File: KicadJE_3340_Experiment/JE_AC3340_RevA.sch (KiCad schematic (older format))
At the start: 99 parts

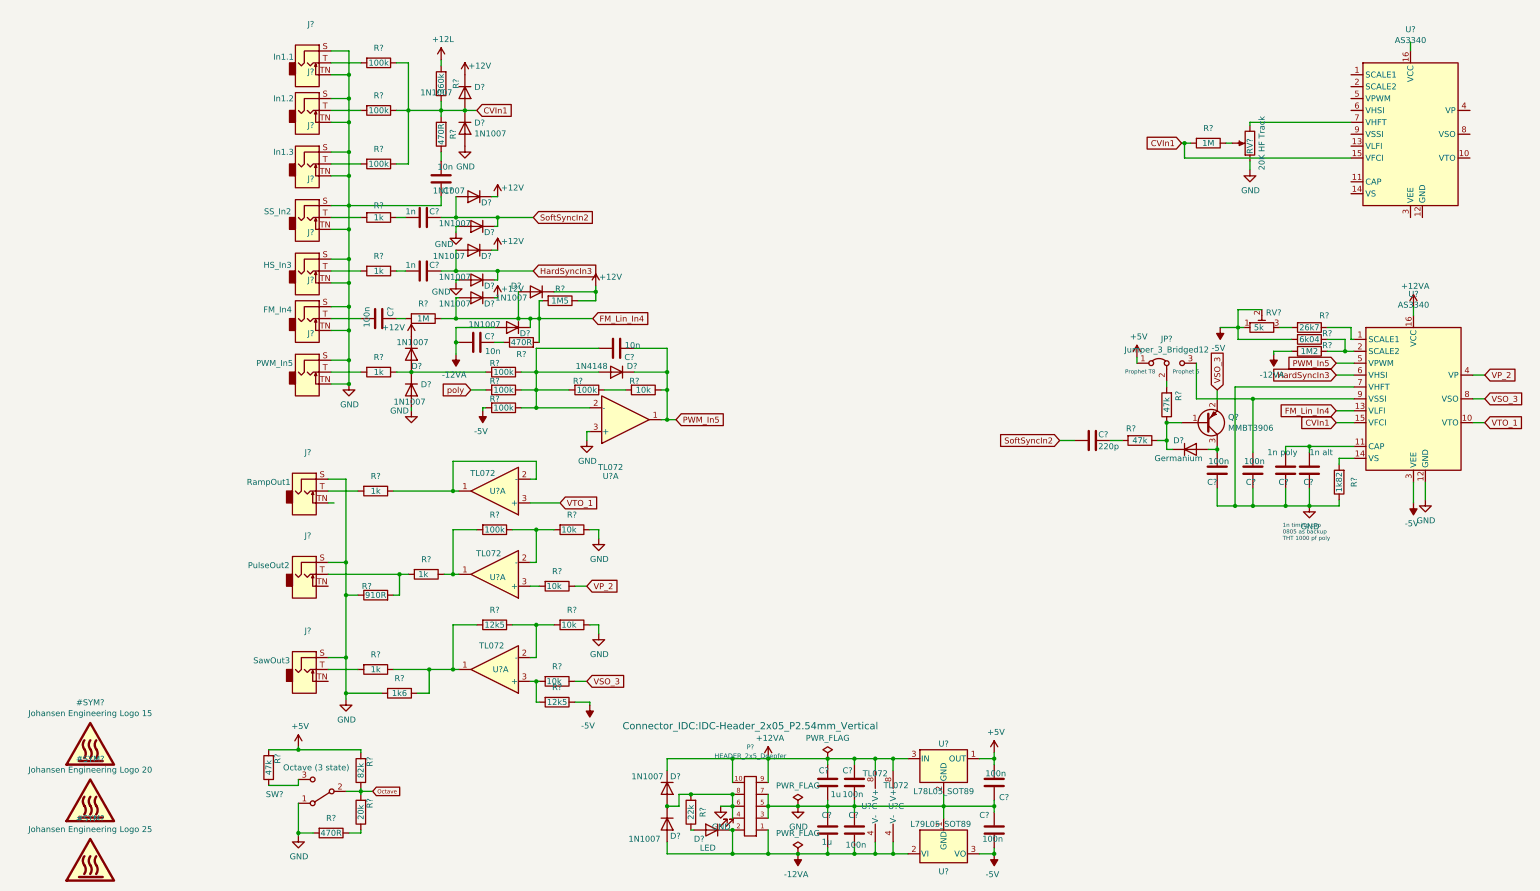
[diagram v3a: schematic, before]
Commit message: Label JE 3 + Pot's
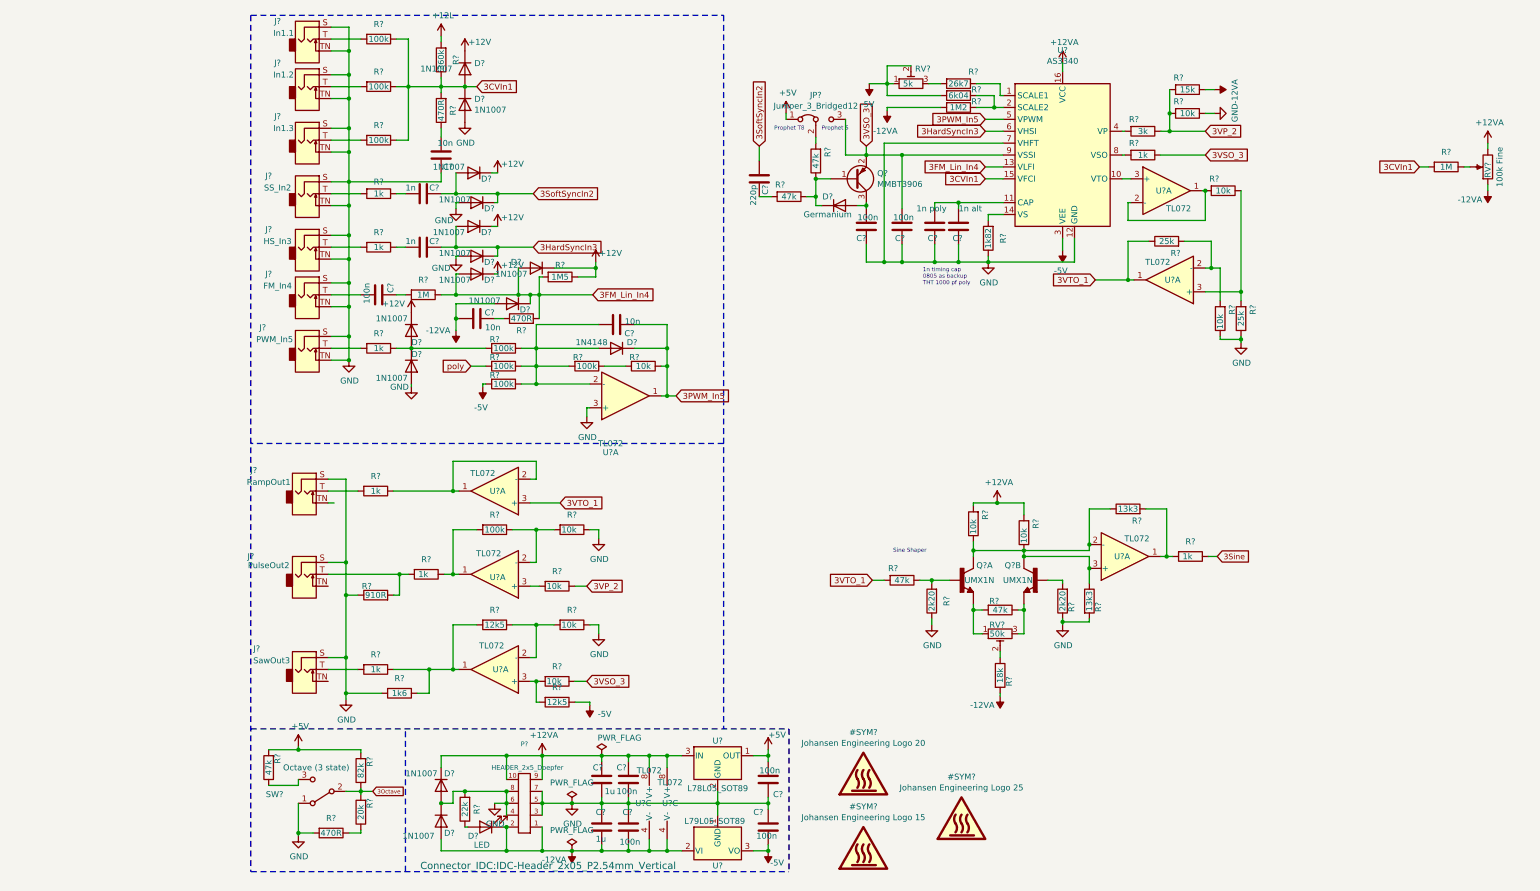
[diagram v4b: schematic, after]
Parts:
- removed U?: AS3340, symbol Audio:AS3340
- added Q? (x2): UMX1N, UMT6, symbol UMX1N:UMX1N
- added R?: 3k, Resistor_SMD:R_0805_2012Metric_Pad1.15x1.40mm_HandSolder, symbol Device:R
- added R? (x2): 1k, Resistor_SMD:R_0805_2012Metric_Pad1.15x1.40mm_HandSolder, symbol Device:R
- added R? (x5): 10k, Resistor_SMD:R_0805_2012Metric_Pad1.15x1.40mm_HandSolder, symbol Device:R
- added R?: 15k, Resistor_SMD:R_0805_2012Metric_Pad1.15x1.40mm_HandSolder, symbol Device:R
- added R? (x2): 25k, Resistor_SMD:R_0805_2012Metric_Pad1.15x1.40mm_HandSolder, symbol Device:R
- added R? (x2): 47k, Resistor_SMD:R_0805_2012Metric_Pad1.15x1.40mm_HandSolder, symbol Device:R
- added R? (x2): 2k20, Resistor_SMD:R_0805_2012Metric_Pad1.15x1.40mm_HandSolder, symbol Device:R
- added R? (x2): 13k3, Resistor_SMD:R_0805_2012Metric_Pad1.15x1.40mm_HandSolder, symbol Device:R
- added R?: 18k, Resistor_SMD:R_0805_2012Metric_Pad1.15x1.40mm_HandSolder, symbol Device:R
- added RV?: 50k, Potentiometer_THT:Potentiometer_Bourns_3296W_Vertical, symbol Device:R_POT_TRIM
- added U? (x3): TL072, AJ-Dropbox-Kicad:AJ_SO-8_5.3x6.2mm_P1.27mm, symbol Amplifier_Operational:TL072
- RV?: value 20K HF Track -> 100k Fine
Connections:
- net +12VA: now also RV?.3, R?.2, R?.2
- net -12VA: now also RV?.1, R?.1, R?.2
- net GND: now also R?.1, R?.1, R?.1, R?.1, R?.1, R?.2; no longer RV?.1
- net 3VSO_3: now reaches C?.2, JP?.3 (B), U?.9 (VSSI)
- net 3VSO_3: now also Q?.2 (E), R?.1, R?.1
- net CVIn1 renamed 3CVIn1
- net FM_Lin_In4 renamed 3FM_Lin_In4
- net HardSyncIn3 renamed 3HardSyncIn3
- net Octave renamed 3Octave
- net PWM_In5 renamed 3PWM_In5
- net SoftSyncIn2 renamed 3SoftSyncIn2
- net VP_2: no longer names the net of U?.4 (VP)
- net VP_2: now also R?.2; no longer R?.1
- removed net VSO_3: Q?.2 (E), R?.1, U?.8 (VSO)
- net VTO_1: no longer names the net of U?.10 (VTO)
- net VTO_1: now also U?.3 (+); no longer U?.3 (+)
- new net: R?.2, U?.8 (VSO)
- new net: R?.2, U?.1, U?.2 (-)
- new net: R?.2, R?.2, U?.2 (-)
- new net: R?.1, R?.2, U?.3 (+)
- new net: Q?.2 (B), R?.1, R?.2
- new net: Q?.1 (E), R?.2, RV?.1
- new net: Q?.3 (C), Q?.6 (C), R?.1, R?.1, R?.1, R?.1, U?.2 (-), U?.3 (+)
- new net: Q?.4 (E), R?.1, RV?.3
- new net: Q?.5 (B), R?.2
- new net: R?.2, R?.2, U?.1
- new net: R?.1, RV?.2
- new net 3Sine: R?.1
- new net 3VP_2: R?.1, R?.1, R?.2, R?.2
- new net 3VTO_1: R?.1, R?.2, U?.1, U?.3 (+)
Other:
- note added: "Sine Shaper"
- moved on the sheet: C?, D?, J?, JP?, P?, Q?, R?, RV?, U?, U?A, U?C

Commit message: Update JE_AC3340_RevA.sch
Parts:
- added D? (x2): 1N1007, Diode_SMD:D_SOD-123, symbol Device:D
- added R?: 100k, Resistor_SMD:R_0805_2012Metric_Pad1.15x1.40mm_HandSolder, symbol Device:R
- added RV?: 100k PWM, AJ-Dropbox-Kicad:Potentiometer_China_RK09_Single_Vertical_AJ, symbol Envelope-cache-2018-08-04-13-00-04:POT
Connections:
- net +12VA: now also D?.1 (K), RV?.3
- net +5V: now also D?.2 (A)
- net -12VA: now also D?.2 (A)
- net -5V: now also D?.2 (A), D?.1 (K)
- net GND: now also R?.2, RV?.1; no longer D?.2 (A), R?.1
- net at R?.2, U?.2 (-): now also R?.1; no longer R?.2
- net poly renamed 3PWM_Adj
- net 3PWM_Adj: now also R?.2
- new net: R?.1, RV?.2
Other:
- note added: "AS 3340 and Sync"
- note added: "Freq Manual Adjust"
- note added: "Input"
- note added: "Octave Adjust"
- note added: "Output"
- note added: "PWM Manual Adjust"
- note added: "Power"
- moved on the sheet: C?, D?, P?, Q?A, Q?B, R?, RV?, SW?, U?, U?A, U?C

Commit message: Update JE_AC3340_RevA.sch
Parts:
- added R?: 1k, Resistor_SMD:R_0805_2012Metric_Pad1.15x1.40mm_HandSolder, symbol Device:R
- added R?: OPEN, Resistor_SMD:R_0805_2012Metric_Pad1.15x1.40mm_HandSolder, symbol Device:R
- added U?: TL072, AJ-Dropbox-Kicad:AJ_SO-8_5.3x6.2mm_P1.27mm, symbol Amplifier_Operational:TL072
- R?: value 47k -> 390R
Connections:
- net 3CVIn1: now also R?.1; no longer D?.1 (K), D?.2 (A), R?.1, R?.1, R?.1, R?.1, R?.2
- net 3VTO_1: now also U?.5 (+), U?.7; no longer U?.1, U?.3 (+)
- net at R?.1, R?.1, R?.2: now also U?.7; no longer U?.1
- net at R?.1, R?.2: now also U?.6 (-); no longer U?.2 (-) (x2)
- net at R?.2, R?.2: now also U?.5 (+); no longer U?.3 (+)
- net at R?.1, R?.2: now also U?.5 (+); no longer U?.3 (+)
- net at Q?.3 (C), Q?.6 (C), R?.1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: now also U?.5 (+), U?.6 (-); no longer U?.2 (-), U?.3 (+)
- net at R?.2, R?.2: now also U?.7; no longer U?.1
- new net: D?.1 (K), D?.2 (A), R?.1, R?.1, R?.1, R?.1, R?.2, R?.2, U?.3 (+)
- new net: R?.1, U?.6 (-), U?.7
- new net: R?.1, R?.2, U?.1, U?.2 (-)
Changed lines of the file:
@@
 Wire Wire Line
 	1350 1225 1350 1025
-Text GLabel 2425 1125 2    50   Input ~ 0
+Text GLabel 3750 1225 2    50   Input ~ 0
 3CVIn1
 Wire Wire Line
@@
 Connection ~ 2325 1125
 Wire Wire Line
-	2325 1125 2425 1125
-Wire Wire Line
 	2125 1125 2325 1125
 Wire Wire Line
@@
 $Comp
 L Amplifier_Operational:TL072 U?
-U 1 1 5F7CE424
+U 2 1 5F7CE424
 P 2575 4525
 AR Path="/5D99B81E/5F7CE424" Ref="U?"  Part="3"
@@
 AR Path="/5F18E4B5/5F7CE424" Ref="U?"  Part="2"
 AR Path="/5E62ACA1/5F7CE424" Ref="U?"  Part="1"
-AR Path="/5F49A670/5F7CE424" Ref="U?"  Part="1"
+AR Path="/5F49A670/5F7CE424" Ref="U?"  Part="2"
 F 0 "U?" H 2600 4500 50  0000 C CNN
 F 1 "TL072" H 2550 4575 50  0000 C CNN
 F 2 "AJ-Dropbox-Kicad:AJ_SO-8_5.3x6.2mm_P1.27mm" H 2575 4525 50  0001 C CNN
 F 3 "http://www.ti.com/lit/ds/symlink/tl071.pdf" H 2575 4525 50  0001 C CNN
-	1    2575 4525
+	2    2575 4525
 	-1   0    0    1
 $EndComp
@@
 $Comp
 L Amplifier_Operational:TL072 U?
-U 1 1 5FE7E2ED
+U 2 1 5FE7E2ED
 P 2575 6025
 AR Path="/5D99B81E/5FE7E2ED" Ref="U?"  Part="3"
@@
 AR Path="/5F18E4B5/5FE7E2ED" Ref="U?"  Part="2"
 AR Path="/5E62ACA1/5FE7E2ED" Ref="U?"  Part="1"
-AR Path="/5F49A670/5FE7E2ED" Ref="U?"  Part="1"
+AR Path="/5F49A670/5FE7E2ED" Ref="U?"  Part="2"
 F 0 "U?" H 2550 5975 50  0000 C CNN
 F 1 "TL072" H 2525 6050 50  0000 C CNN
 F 2 "AJ-Dropbox-Kicad:AJ_SO-8_5.3x6.2mm_P1.27mm" H 2575 6025 50  0001 C CNN
 F 3 "http://www.ti.com/lit/ds/symlink/tl071.pdf" H 2575 6025 50  0001 C CNN
-	1    2575 6025
+	2    2575 6025
 	-1   0    0    1
 $EndComp
@@
 $Comp
 L Amplifier_Operational:TL072 U?
-U 1 1 6058F368
+U 2 1 6058F368
 P 9625 2100
 AR Path="/5D99B81E/6058F368" Ref="U?"  Part="3"
@@
 AR Path="/5F18E4B5/6058F368" Ref="U?"  Part="2"
 AR Path="/5E62ACA1/6058F368" Ref="U?"  Part="1"
-AR Path="/5F49A670/6058F368" Ref="U?"  Part="1"
+AR Path="/5F49A670/6058F368" Ref="U?"  Part="2"
 F 0 "U?" H 9575 2100 50  0000 C CNN
 F 1 "TL072" H 9725 1950 50  0000 C CNN
 F 2 "AJ-Dropbox-Kicad:AJ_SO-8_5.3x6.2mm_P1.27mm" H 9625 2100 50  0001 C CNN
 F 3 "http://www.ti.com/lit/ds/symlink/tl071.pdf" H 9625 2100 50  0001 C CNN
-	1    9625 2100
+	2    9625 2100
 	1    0    0    -1
 $EndComp
@@
 $Comp
 L Amplifier_Operational:TL072 U?
-U 1 1 6091B290
+U 2 1 6091B290
 P 7200 3525
 AR Path="/5D99B81E/6091B290" Ref="U?"  Part="3"
@@
 AR Path="/5F18E4B5/6091B290" Ref="U?"  Part="2"
 AR Path="/5E62ACA1/6091B290" Ref="U?"  Part="1"
-AR Path="/5F49A670/6091B290" Ref="U?"  Part="1"
+AR Path="/5F49A670/6091B290" Ref="U?"  Part="2"
 F 0 "U?" H 7075 3475 50  0000 C CNN
 F 1 "TL072" H 7125 3550 50  0000 C CNN
 F 2 "AJ-Dropbox-Kicad:AJ_SO-8_5.3x6.2mm_P1.27mm" H 7200 3525 50  0001 C CNN
 F 3 "http://www.ti.com/lit/ds/symlink/tl071.pdf" H 7200 3525 50  0001 C CNN
-	1    7200 3525
+	2    7200 3525
 	1    0    0    1
 $EndComp
@@
 AR Path="/5F49A670/60B03485" Ref="R?"  Part="1"
 F 0 "R?" V 6075 3925 50  0000 C CNN
-F 1 "47k" V 6150 3975 50  0000 C CNN
+F 1 "390R" V 6150 3975 50  0000 C CNN
 F 2 "Resistor_SMD:R_0805_2012Metric_Pad1.15x1.40mm_HandSolder" V 6080 3975 50  0001 C CNN
 F 3 "~" H 6150 3975 50  0001 C CNN
@@
 Text Notes 1325 6625 0    50   ~ 0
 Octave Adjust
+$Comp
+L Amplifier_Operational:TL072 U?
+U 1 1 614891B3
+P 3050 1225
+AR Path="/5D99B81E/614891B3" Ref="U?"  Part="3"
+AR Path="/5D99B7BA/614891B3" Ref="U?"  Part="1"
+AR Path="/5F18E4B5/614891B3" Ref="U?"  Part="2"
+AR Path="/5E62ACA1/614891B3" Ref="U?"  Part="1"
+AR Path="/5F49A670/614891B3" Ref="U?"  Part="1"
+F 0 "U?" H 2950 1250 50  0000 C CNN
+F 1 "TL072" H 2975 1175 50  0000 C CNN
+F 2 "AJ-Dropbox-Kicad:AJ_SO-8_5.3x6.2mm_P1.27mm" H 3050 1225 50  0001 C CNN
+F 3 "http://www.ti.com/lit/ds/symlink/tl071.pdf" H 3050 1225 50  0001 C CNN
+	1    3050 1225
+	1    0    0    -1
+$EndComp
+Wire Wire Line
+	2750 1325 2725 1325
+Wire Wire Line
+	2725 1325 2725 1475
+Wire Wire Line
+	2725 1475 3375 1475
+Wire Wire Line
+	3375 1475 3375 1225
+Wire Wire Line
+	3375 1225 3350 1225
+$Comp
+L Device:R R?
+U 1 1 614891BF
+P 3525 1225
+AR Path="/614891BF" Ref="R?"  Part="1"
+AR Path="/5C8C5FC0/614891BF" Ref="R?"  Part="1"
+AR Path="/5CAAE8D3/614891BF" Ref="R?"  Part="1"
+AR Path="/5E4B0DD9/614891BF" Ref="R?"  Part="1"
+AR Path="/5E62ACA1/614891BF" Ref="R?"  Part="1"
+AR Path="/5F49A670/614891BF" Ref="R?"  Part="1"
+F 0 "R?" V 3425 1150 50  0000 C CNN
+F 1 "1k" V 3525 1225 50  0000 C CNN
+F 2 "Resistor_SMD:R_0805_2012Metric_Pad1.15x1.40mm_HandSolder" V 3455 1225 50  0001 C CNN
+F 3 "~" H 3525 1225 50  0001 C CNN
+	1    3525 1225
+	0    1    1    0
+$EndComp
+Connection ~ 3375 1225
+Wire Wire Line
+	2325 1125 2725 1125
+Wire Wire Line
+	3750 1225 3675 1225
+$Comp
+L Device:R R?
+U 1 1 61551447
+P 3050 900
+AR Path="/61551447" Ref="R?"  Part="1"
+AR Path="/5C8C5FC0/61551447" Ref="R?"  Part="1"
+AR Path="/5CAAE8D3/61551447" Ref="R?"  Part="1"
+AR Path="/5E4B0DD9/61551447" Ref="R?"  Part="1"
+AR Path="/5E62ACA1/61551447" Ref="R?"  Part="1"
+AR Path="/5F49A670/61551447" Ref="R?"  Part="1"
+F 0 "R?" V 2950 825 50  0000 C CNN
+F 1 "OPEN" V 3050 900 50  0000 C CNN
+F 2 "Resistor_SMD:R_0805_2012Metric_Pad1.15x1.40mm_HandSolder" V 2980 900 50  0001 C CNN
+F 3 "~" H 3050 900 50  0001 C CNN
+	1    3050 900
+	0    1    1    0
+$EndComp
+Wire Wire Line
+	2725 1125 2725 900
+Wire Wire Line
+	2725 900  2900 900
+Connection ~ 2725 1125
+Wire Wire Line
+	2725 1125 2750 1125
+Wire Wire Line
+	3375 1225 3375 900
+Wire Wire Line
+	3375 900  3200 900
 $EndSCHEMATC

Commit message: Update JE_AC3340_RevA.sch
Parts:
- added J?: PWM_In5, AJ-Dropbox-Kicad:PJ301SM, symbol Connector:AudioJack2_SwitchT
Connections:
- net 3Sine: now also J?.T
- net GND: now also J?.S
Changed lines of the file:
@@
 Wire Wire Line
 	3375 900  3200 900
+$Comp
+L Envelope-cache-2018-08-04-13-00-04:GND #PWR?
+U 1 1 615A670C
+P 7525 4425
+AR Path="/615A670C" Ref="#PWR?"  Part="1"
+AR Path="/5C8C5FC0/615A670C" Ref="#PWR?"  Part="1"
+AR Path="/5CAAE8D3/615A670C" Ref="#PWR?"  Part="1"
+AR Path="/5E4B0DD9/615A670C" Ref="#PWR?"  Part="1"
+AR Path="/5F49A670/615A670C" Ref="#PWR?"  Part="1"
+F 0 "#PWR?" H 7525 4175 50  0001 C CNN
+F 1 "GND" H 7530 4252 50  0000 C CNN
+F 2 "" H 7525 4425 50  0001 C CNN
+F 3 "" H 7525 4425 50  0001 C CNN
+	1    7525 4425
+	-1   0    0    -1
+$EndComp
+$Comp
+L Connector:AudioJack2_SwitchT J?
+U 1 1 615A6716
+P 7875 4325
+AR Path="/615A6716" Ref="J?"  Part="1"
+AR Path="/5C8C5FC0/615A6716" Ref="J?"  Part="1"
+AR Path="/5CAAE8D3/615A6716" Ref="J?"  Part="1"
+AR Path="/5E4B0DD9/615A6716" Ref="J?"  Part="1"
+AR Path="/5F49A670/615A6716" Ref="J?"  Part="1"
+F 0 "J?" H 7500 4500 50  0000 C CNN
+F 1 "PWM_In5" H 7600 4400 50  0000 C CNN
+F 2 "AJ-Dropbox-Kicad:PJ301SM" H 7875 4325 50  0001 C CNN
+F 3 "~" H 7875 4325 50  0001 C CNN
+	1    7875 4325
+	-1   0    0    -1
+$EndComp
+Wire Wire Line
+	7675 4325 7425 4325
+Wire Wire Line
+	7525 4225 7525 4425
+Wire Wire Line
+	7675 4225 7525 4225
+Text GLabel 7425 4325 0    47   Input ~ 0
+3Sine
 $EndSCHEMATC

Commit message: Update JE_AC3340_RevA.sch
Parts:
- J?: value PWM_In5 -> SineOut4
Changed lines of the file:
@@
 AR Path="/5F49A670/615A6716" Ref="J?"  Part="1"
 F 0 "J?" H 7500 4500 50  0000 C CNN
-F 1 "PWM_In5" H 7600 4400 50  0000 C CNN
+F 1 "SineOut4" H 7600 4400 50  0000 C CNN
 F 2 "AJ-Dropbox-Kicad:PJ301SM" H 7875 4325 50  0001 C CNN
 F 3 "~" H 7875 4325 50  0001 C CNN
